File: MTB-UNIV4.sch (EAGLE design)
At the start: 132 parts, among them IC1 MEGA128-A, IC2 SN75176BP, IC3 MC7805CDTG, IC4 ULN2803A, IC5 ULN2803A, Q1 14.7456 MHz, X1A ARK500/2, X1B ARK500/2, X2A ARK500/2, X2B ARK500/2, X3 1751316, X4 1751316, X5 1751316, X6 1751316

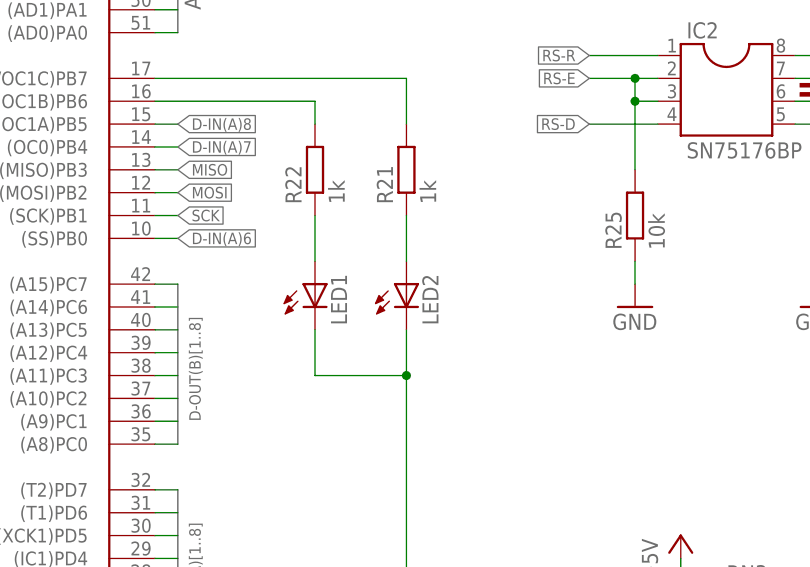
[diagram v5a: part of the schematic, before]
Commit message: Add LEDs color.
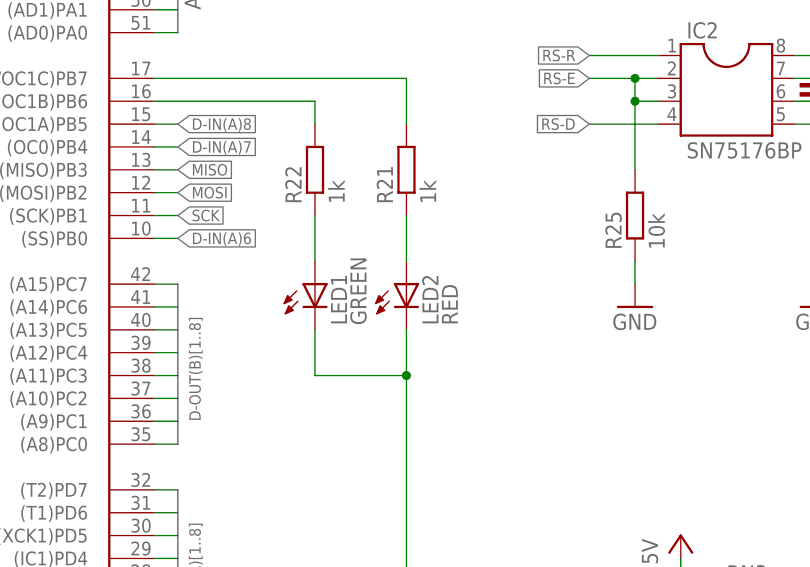
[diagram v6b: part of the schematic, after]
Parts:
- LED1: value (none) -> GREEN
- LED2: value (none) -> RED
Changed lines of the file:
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@@
 <part name="D2" library="diode" library_urn="urn:adsk.eagle:library:210" deviceset="ZENER-DIODE" device="SOT23" package3d_urn="urn:adsk.eagle:package:43389/2" value="15V"/>
 <part name="IC3" library="LDO" library_urn="urn:adsk.eagle:library:20959563" deviceset="MC78M05BDTRKG" device="" package3d_urn="urn:adsk.eagle:package:20920771/3" value="MC7805CDTG"/>
-<part name="LED1" library="adafruit" library_urn="urn:adsk.eagle:library:420" deviceset="LED" device="CHIPLED_1206" package3d_urn="urn:adsk.eagle:package:6240560/1"/>
-<part name="LED2" library="adafruit" library_urn="urn:adsk.eagle:library:420" deviceset="LED" device="CHIPLED_1206" package3d_urn="urn:adsk.eagle:package:6240560/1"/>
+<part name="LED1" library="adafruit" library_urn="urn:adsk.eagle:library:420" deviceset="LED" device="CHIPLED_1206" package3d_urn="urn:adsk.eagle:package:6240560/1" value="GREEN"/>
+<part name="LED2" library="adafruit" library_urn="urn:adsk.eagle:library:420" deviceset="LED" device="CHIPLED_1206" package3d_urn="urn:adsk.eagle:package:6240560/1" value="RED"/>
 <part name="R21" library="rcl" deviceset="R-EU_" device="R1206" value="1k"/>
 <part name="R22" library="rcl" deviceset="R-EU_" device="R1206" value="1k"/>

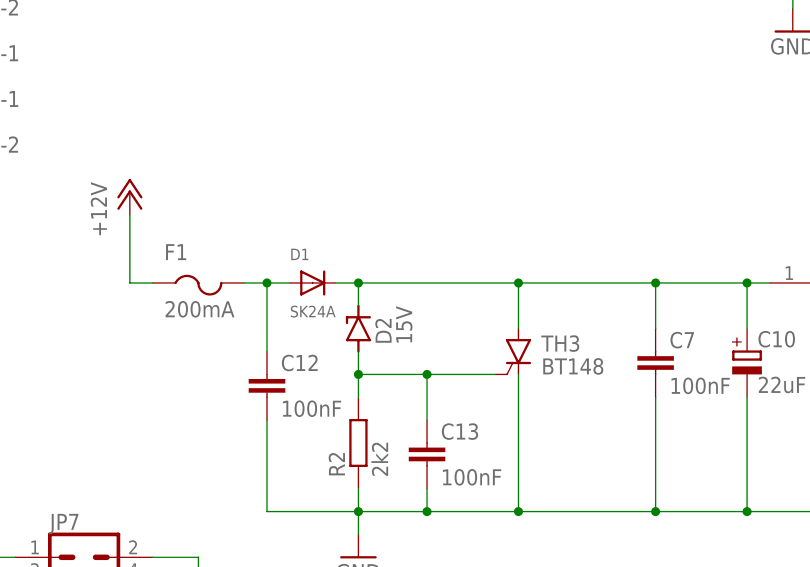
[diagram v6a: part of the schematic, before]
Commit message: Add diode value.
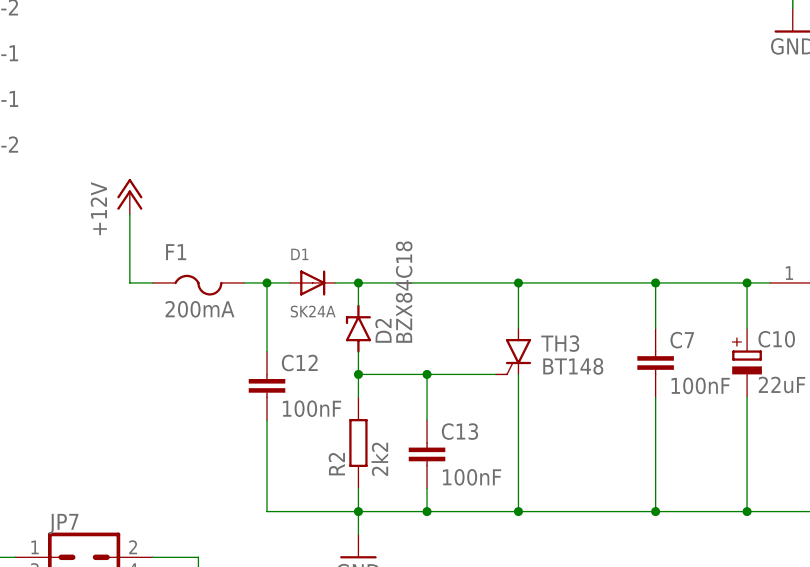
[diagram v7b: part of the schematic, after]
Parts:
- D2: value 15V -> BZX84C18
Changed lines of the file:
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@@
 <part name="TH3" library="ElectroKrt" deviceset="BT148" device="" package3d_urn="urn:adsk.eagle:package:30370/1" value="BT148"/>
 <part name="C13" library="rcl" deviceset="C-EU" device="C1206" value="100nF"/>
-<part name="D2" library="diode" library_urn="urn:adsk.eagle:library:210" deviceset="ZENER-DIODE" device="SOT23" package3d_urn="urn:adsk.eagle:package:43389/2" value="15V"/>
+<part name="D2" library="diode" library_urn="urn:adsk.eagle:library:210" deviceset="ZENER-DIODE" device="SOT23" package3d_urn="urn:adsk.eagle:package:43389/2" value="BZX84C18"/>
 <part name="IC3" library="LDO" library_urn="urn:adsk.eagle:library:20959563" deviceset="MC78M05BDTRKG" device="" package3d_urn="urn:adsk.eagle:package:20920771/3" value="MC7805CDTG"/>
 <part name="LED1" library="adafruit" library_urn="urn:adsk.eagle:library:420" deviceset="LED" device="CHIPLED_1206" package3d_urn="urn:adsk.eagle:package:6240560/1" value="GREEN"/>
